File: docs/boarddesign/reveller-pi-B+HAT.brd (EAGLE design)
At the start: 65 x 56 mm, 23 parts, among them IC100 6581, Q100 IRF9Z24N, T100 BC547, X1 RASPI_BOARD_B+#_HDC, X101 PG203J, X102 CANTON-POWER

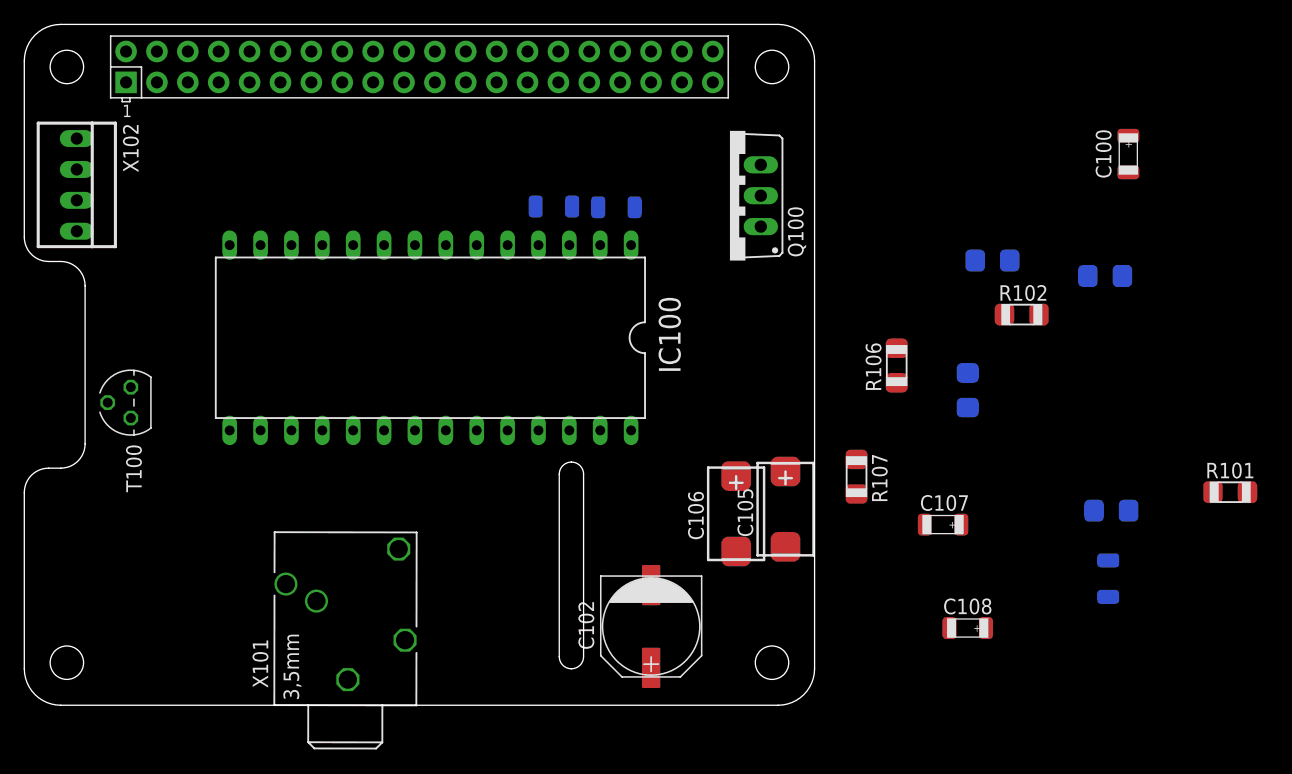
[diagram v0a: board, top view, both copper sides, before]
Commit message: Added box design and revised RevellerZero design
Raspberry Pi Rev B box design to allow for reveller HAT. Can be printed
with or without vented design. Designed in Solidworks 2016. RevellerZero
board design was revised due to CantonPower being placed slightly off
board.
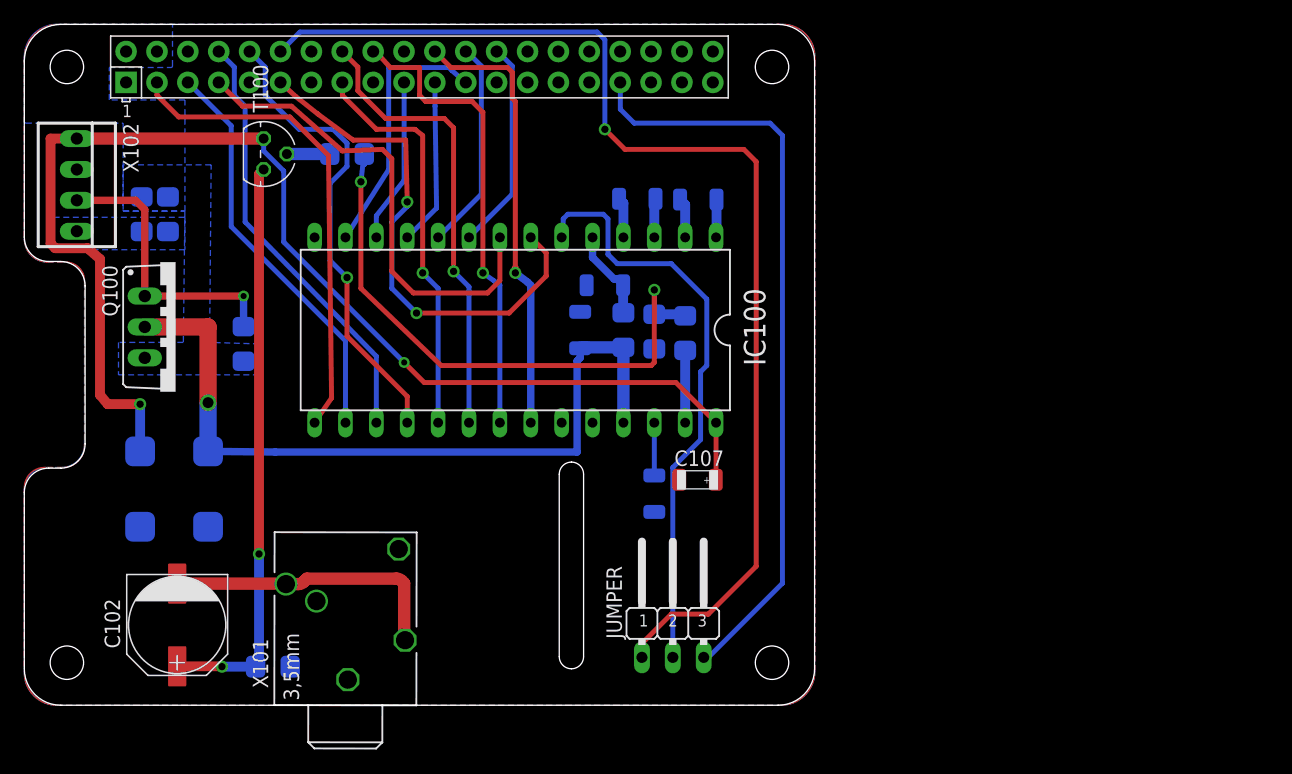
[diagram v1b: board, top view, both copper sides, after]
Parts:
- added JUMPER: (no value), jumper:JP2W
- moved R101 80.0 mm to (20.4, 3.17), flipped to the bottom, turned to 180 degrees
- moved R105 71.1 mm to (18.0, 29.7), turned to 270 degrees
- moved R106 63.3 mm to (9.65, 40.4), flipped to the bottom
- moved R107 60.6 mm to (11.8, 40.4), flipped to the bottom
- moved R104 54.6 mm to (26.5, 45.3), turned to 0 degrees
- moved C105 53.1 mm to (9.53, 17.8), flipped to the bottom
- moved Q100 46.9 mm to (12.4, 31.1), turned to 270 degrees
- moved C100 44.4 mm to (47.8, 34.5), flipped to the bottom, turned to 0 degrees
- moved C106 43.5 mm to (15.1, 17.8), flipped to the bottom
- moved R100 40.4 mm to (51.8, 30.7), turned to 90 degrees
- moved C108 40.2 mm to (45.7, 30.9), flipped to the bottom, turned to 270 degrees
- moved C102 39.0 mm to (12.6, 6.60)
- moved C101 38.0 mm to (51.8, 17.4)
- moved R102 32.8 mm to (49.3, 30.9), flipped to the bottom, turned to 270 degrees
- moved R103 26.0 mm to (54.4, 30.6), turned to 90 degrees
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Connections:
- net N$1 renamed 5VSTABIL
- new net CLKOC1: JUMPER.3, X1.33
- new net CLKRPI: JUMPER.1, X1.12
- new net PWCTLRPI: Q100.G, R105.1, X102.3
- net A0: now also X1.26
- net A1: now also X1.24
- net A2: now also X1.21
- net A3: now also X1.19
- net A4: now also X1.23
- net CLK: now also JUMPER.2; no longer X1.12
- net PWCTL: no longer Q100.G, R105.1, X102.3
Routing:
- net +12V: track 0.00 -> 105.1 mm, vias 0 -> 2
- net CLKRPI: track 0.00 -> 95.0 mm, vias 0 -> 1
- net +5V_SID: track 0.00 -> 64.2 mm, vias 0 -> 1
- net CLKOC1: track 0.00 -> 62.3 mm
- net AUDIO_PREAMP: track 0.00 -> 50.2 mm, vias 0 -> 2
- net CLK: track 0.00 -> 48.8 mm
- net AUDIO_DC: track 0.00 -> 47.5 mm, vias 0 -> 2
- net RW: track 0.00 -> 43.2 mm, vias 0 -> 2
- net CS: track 0.00 -> 39.6 mm
- net D0: track 0.00 -> 39.6 mm
- net D6: track 0.00 -> 38.7 mm, vias 0 -> 1
- net D3: track 0.00 -> 38.7 mm, vias 0 -> 1
- net D5: track 0.00 -> 37.7 mm, vias 0 -> 1
- net D7: track 0.00 -> 36.6 mm, vias 0 -> 1
- net D2: track 0.00 -> 35.8 mm
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- added copper zone on layer 16, net +5V
- added copper zone on layer 16, net 5VSTABIL
- added copper zone on layer 1, net GND
- added copper zone on layer 16, net GND
